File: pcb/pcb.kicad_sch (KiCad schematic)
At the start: 0 parts

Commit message: Finished Zen Part 1
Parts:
- added C1, C2, C3, C4, C5: 0.1u, symbol Device:C_Small
- added C1: 1u, symbol Device:C_Small
- added C2, C3: 22p, symbol Device:C_Small
- added F1: 500m, symbol Device:Polyfuse_Small
- added J1: AVR-ISP-6, symbol Connector:AVR-ISP-6
- added R1, R3: 10k, symbol Device:R_Small
- added R4, R5: 22, symbol Device:R_Small
- added R6, R7: 5.1k, symbol Device:R_Small
- added U1: ATmega32U4-A, Package_QFP:TQFP-44_10x10mm_P0.8mm, symbol MCU_Microchip_ATmega:ATmega32U4-A
- added U2: PRTR5V0U2X, symbol random-keyboard-parts:PRTR5V0U2X
- added USB1: HRO-TYPE-C-31-M-12, symbol Type-C:HRO-TYPE-C-31-M-12
- added Y1: Crystal_GND24_Small, symbol Device:Crystal_GND24_Small
- added r2: ~, symbol local:SW_SKQG
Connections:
- new net: C1.1, C2.1, C4.1, C5.1
- new net: C1.2, C2.2, C4.2, C5.2
- new net: R4.1, U2.3 (IO2), USB1.5 (DN2), USB1.7 (DN1)
- new net: R1.1, U1.33 (~{HWB}/PE2)
- new net: C1.1, U1.6 (UCAP)
- new net: R6.2, USB1.10 (CC2)
- new net: R7.1, USB1.4 (CC1)
- new net: R5.2, U2.2 (IO1), USB1.6 (DP1), USB1.8 (DP2)
- new net +5V: C3.1, F1.2, J1.2 (VCC), R3.1, U1.14 (VCC), U1.2 (UVCC), U1.24 (AVCC), U1.34 (VCC), U1.44 (AVCC)
- new net D+: R5.1, U1.4 (D+)
- new net D-: R4.2, U1.3 (D-)
- new net GND: C1.2, C2.2, C3.2, C3.2, J1.6 (GND), R1.2, R6.1, R7.2, U1.15 (GND), U1.23 (GND), U1.35 (GND), U1.43 (GND), U1.5 (UGND), U2.1 (GND), USB1.1 (GND), USB1.12 (GND), USB1.13 (SHIELD), Y1.2, Y1.4, r2.2
- new net MISO: J1.1 (MISO), U1.11 (PB3)
- new net MOSI: J1.4 (MOSI), U1.10 (PB2)
- new net RESET: J1.5 (~{RST}), R3.2, r2.1
- new net SCK: J1.3 (SCK), U1.9 (PB1)
- new net VCC: F1.1, U1.7 (VBUS), U2.4 (VCC), USB1.11 (VBUS), USB1.2 (VBUS)
- new net XTAL1: C2.1, U1.17 (XTAL1), Y1.1
- new net XTAL2: C3.1, U1.16 (XTAL2), Y1.3
- no-connect marks 0 -> 6

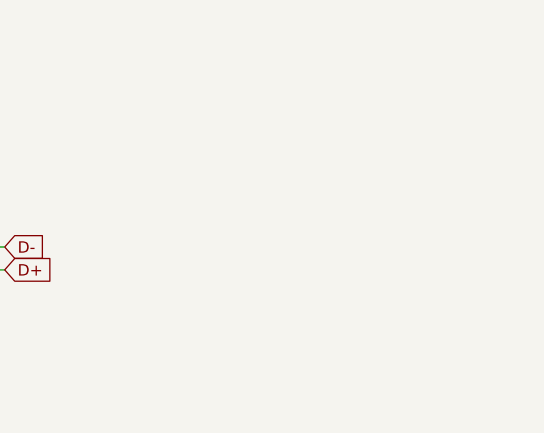
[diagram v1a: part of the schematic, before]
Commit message: Keyboard Switch Matrix Completed
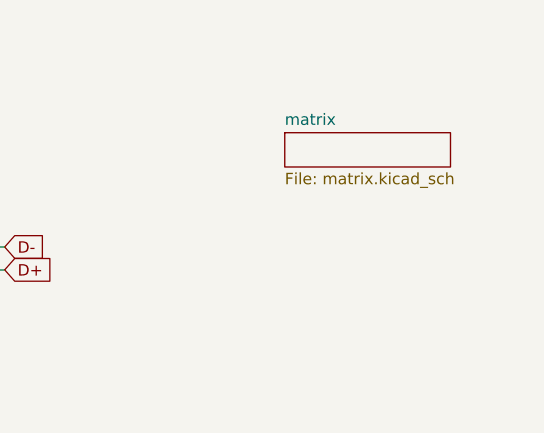
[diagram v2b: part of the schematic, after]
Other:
- added sheet matrix (matrix.kicad_sch)
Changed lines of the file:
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@@
+		)
+	)
+	(sheet
+		(at 197.485 25.4)
+		(size 18.415 3.81)
+		(exclude_from_sim no)
+		(in_bom yes)
+		(on_board yes)
+		(dnp no)
+		(fields_autoplaced yes)
+		(stroke
+			(width 0.1524)
+			(type solid)
+		)
+		(fill
+			(color 0 0 0 0.0000)
+		)
+		(property "Sheetname" "matrix"
+			(at 197.485 24.6884 0)
+			(effects
+				(font
+					(size 1.27 1.27)
+				)
+				(justify left bottom)
+			)
+		)
+		(property "Sheetfile" "matrix.kicad_sch"
+			(at 197.485 29.7946 0)
+			(effects
+				(font
+					(size 1.27 1.27)
+				)
+				(justify left top)
+			)
+		)
+		(instances
+			(project "pcb"
+				(path "/e1222693-dcfd-476e-8f65-9fae5310e84d"
+					(page "2")
+				)
+			)
 		)
 	)

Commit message: Saving Progress on Part 2
Just started the footprint stuff for the switches. Need to make a decision on the switches I want for the keyboard.
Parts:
- C1, C2, C3: footprint (none) -> Capacitor_SMD:C_0805_2012Metric_Pad1.18x1.45mm_HandSolder
- C4: renamed from C1; footprint (none) -> Capacitor_SMD:C_0805_2012Metric_Pad1.18x1.45mm_HandSolder
- C5: renamed from C2; footprint (none) -> Capacitor_SMD:C_0805_2012Metric_Pad1.18x1.45mm_HandSolder
- C6: renamed from C3; footprint (none) -> Capacitor_SMD:C_0805_2012Metric_Pad1.18x1.45mm_HandSolder
- C7: renamed from C4; footprint (none) -> Capacitor_SMD:C_0805_2012Metric_Pad1.18x1.45mm_HandSolder
- C8: renamed from C5; footprint (none) -> Capacitor_SMD:C_0805_2012Metric_Pad1.18x1.45mm_HandSolder
- F1: footprint (none) -> Fuse:Fuse_1206_3216Metric_Pad1.42x1.75mm_HandSolder
- J1: footprint (none) -> random-keyboard-parts:Reset_Pretty-Mask
- R1: renamed from R4; footprint (none) -> Resistor_SMD:R_0805_2012Metric_Pad1.20x1.40mm_HandSolder
- R2: renamed from R5; footprint (none) -> Resistor_SMD:R_0805_2012Metric_Pad1.20x1.40mm_HandSolder
- R3: renamed from R6; footprint (none) -> Resistor_SMD:R_0805_2012Metric_Pad1.20x1.40mm_HandSolder
- R4: renamed from R7; footprint (none) -> Resistor_SMD:R_0805_2012Metric_Pad1.20x1.40mm_HandSolder
- R5: renamed from R3; footprint (none) -> Resistor_SMD:R_0805_2012Metric_Pad1.20x1.40mm_HandSolder
- R6: renamed from R1; footprint (none) -> Resistor_SMD:R_0805_2012Metric_Pad1.20x1.40mm_HandSolder
- U1: renamed from U2; footprint (none) -> random-keyboard-parts:SOT143B
- USB1: footprint (none) -> Type-C:HRO-TYPE-C-31-M-12-HandSoldering
- Y1: footprint (none) -> Crystal:Crystal_SMD_3225-4Pin_3.2x2.5mm_HandSoldering
- r7: renamed from r2; footprint (none) -> Button_Switch_SMD:SW_SPST_SKQG_WithStem
- renumbered U1 to U2
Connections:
- net +5V: now also U2.7 (VBUS)
- net RESET: now also U2.13 (~{RESET})
- net VCC: no longer U2.7 (VBUS)
- net row0: now reaches U2.1 (PE6)
- net col8: now reaches U2.19 (PD1)
- net col9: now reaches U2.20 (PD2)
- net col10: now reaches U2.21 (PD3)
- net col12: now reaches U2.22 (PD5)
- net col11: now reaches U2.25 (PD4)
- net col13: now reaches U2.26 (PD6)
- net col14: now reaches U2.27 (PD7)
- net col0: now reaches U2.28 (PB4)
- net col1: now reaches U2.29 (PB5)
- net col2: now reaches U2.30 (PB6)
- net col3: now reaches U2.31 (PC6)
- net col4: now reaches U2.32 (PC7)
- net col6: now reaches U2.36 (PF7)
- net col5: now reaches U2.37 (PF6)
- net row1: now reaches U2.38 (PF5)
- net row4: now reaches U2.39 (PF4)
- net row3: now reaches U2.40 (PF1)
- net row2: now reaches U2.41 (PF0)
- net col7: now reaches U2.8 (PB0)
- no-connect marks 6 -> 7
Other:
- note added: "Key Swtich Matrix"

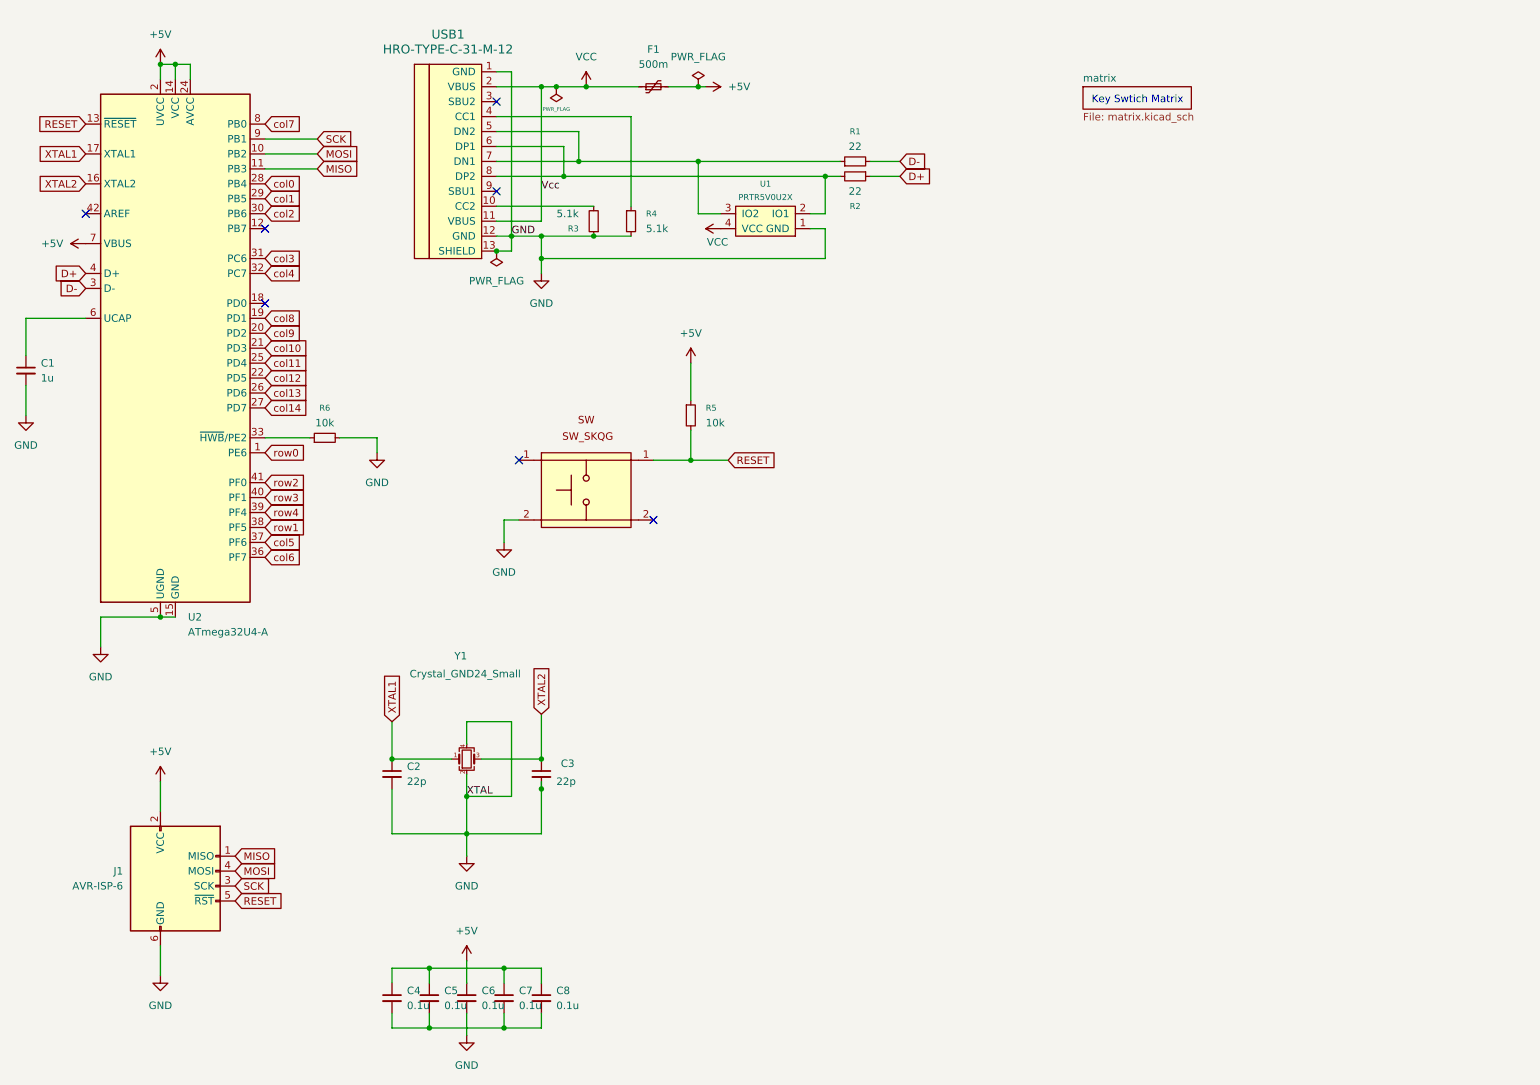
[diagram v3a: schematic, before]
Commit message: Footprints Fix, Layout, and Diode Layout
Fixed a spacing issue with the key switches. Made the control key bigger and then placed diodes. Now saving progress so that I can check that the connections made from the matrix schematic is correct.
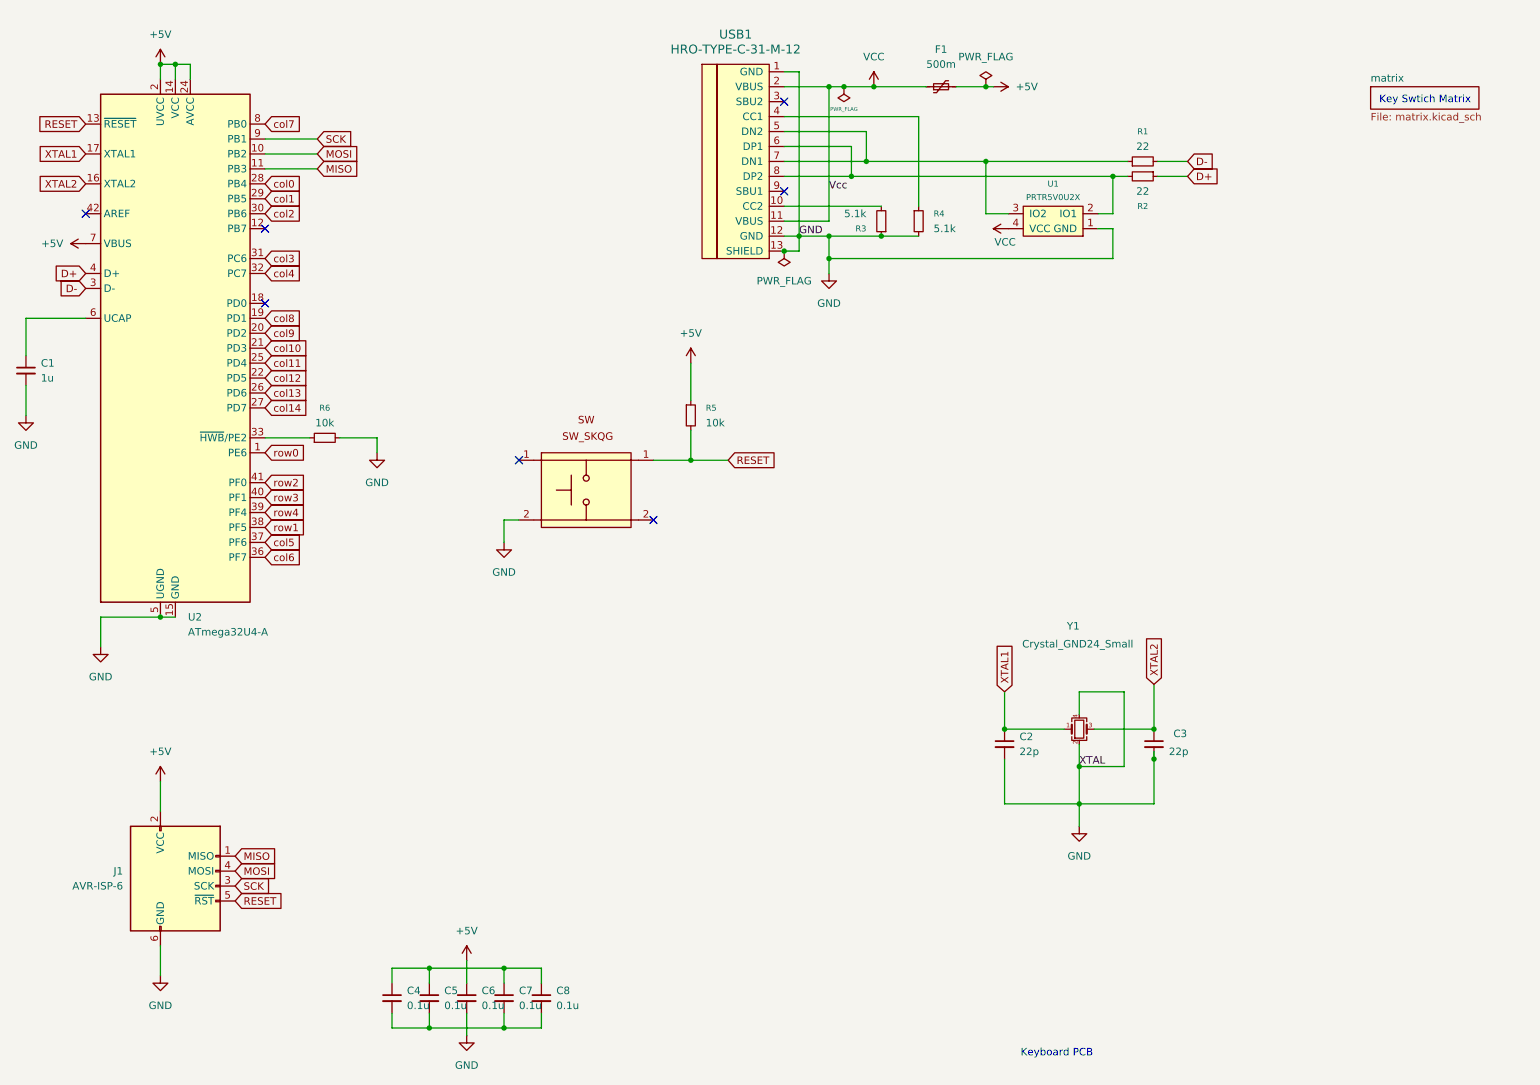
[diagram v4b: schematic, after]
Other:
- note added: "Keyboard PCB"
- moved on the sheet: C2, C3, F1, R1, R2, R3, R4, U1, USB1, Y1

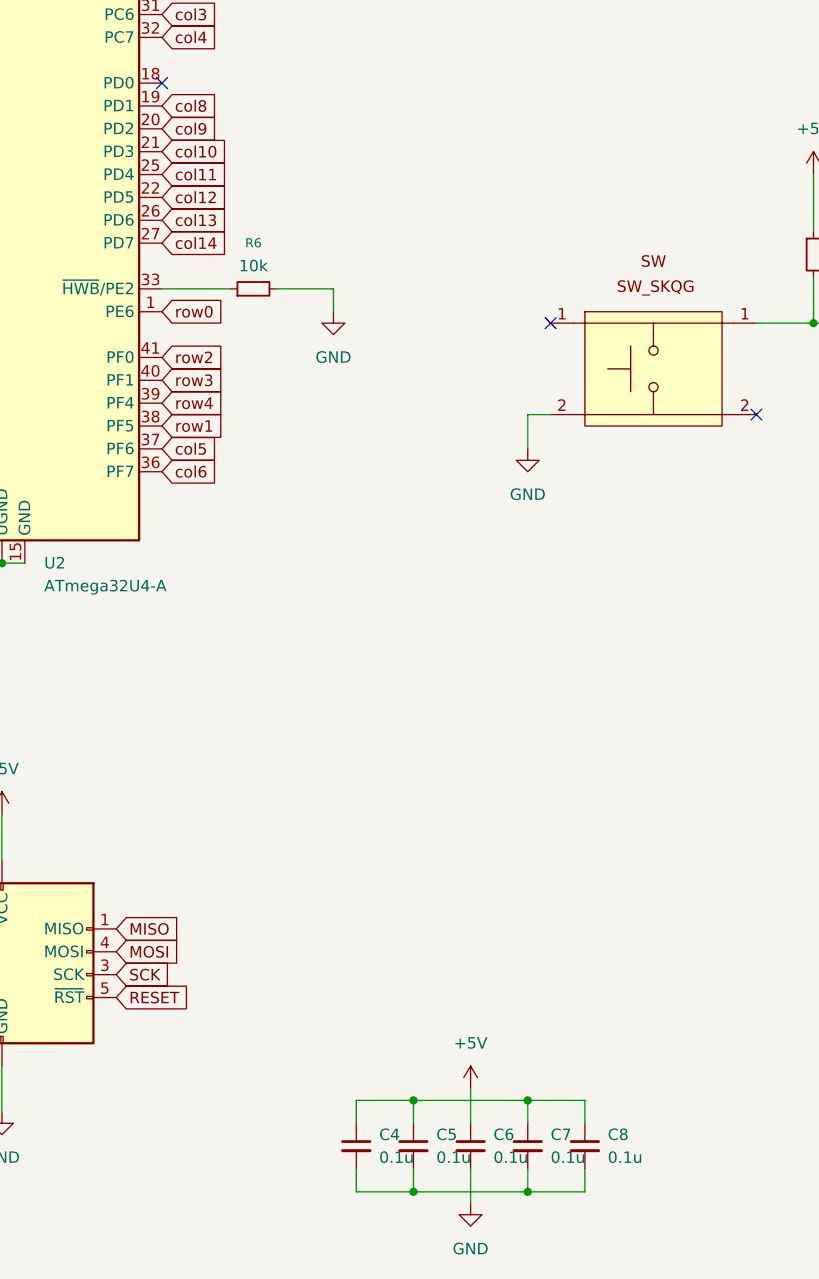
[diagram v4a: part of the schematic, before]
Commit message: Placement of all ICs Finished; Starting Error Checking
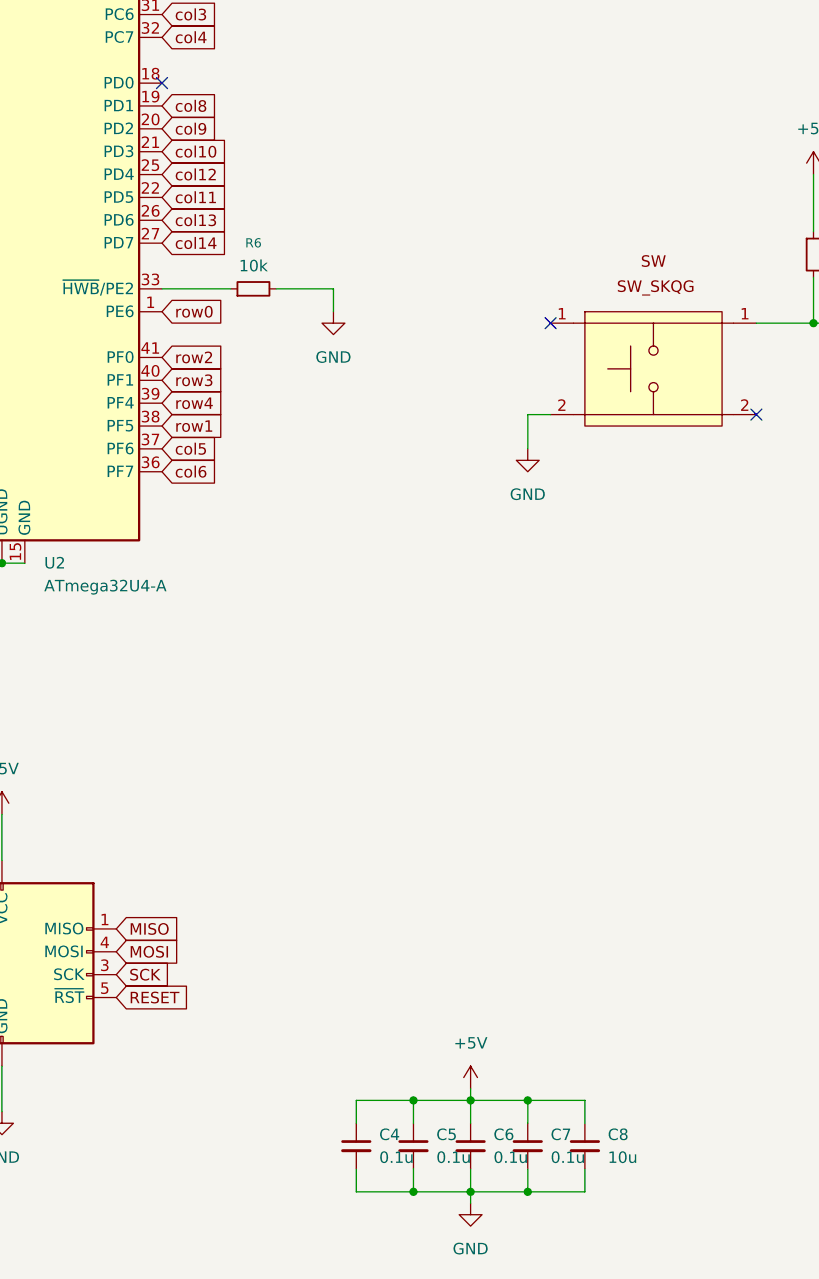
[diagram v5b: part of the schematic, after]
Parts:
- C8: value 0.1u -> 10u
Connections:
- net +5V: now also C4.1, C5.1, C7.1, C8.1
- net GND: now also C4.2, C5.2, C7.2, C8.2
- net col11: now also U2.22 (PD5); no longer U2.25 (PD4)
- net col12: now also U2.25 (PD4); no longer U2.22 (PD5)
